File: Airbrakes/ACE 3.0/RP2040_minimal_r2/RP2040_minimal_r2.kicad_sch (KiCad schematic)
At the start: 45 parts, among them J1 USB_B_Micro, J2 Conn_01x02, J3 104031-0811, J4 Conn_02x18_Odd_Even, J5 104031-0811, U1 NCP1117-3.3_SOT223, U2 W25Q128JVS, U3 RP2040, U4 BMI088, U5 BMP581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

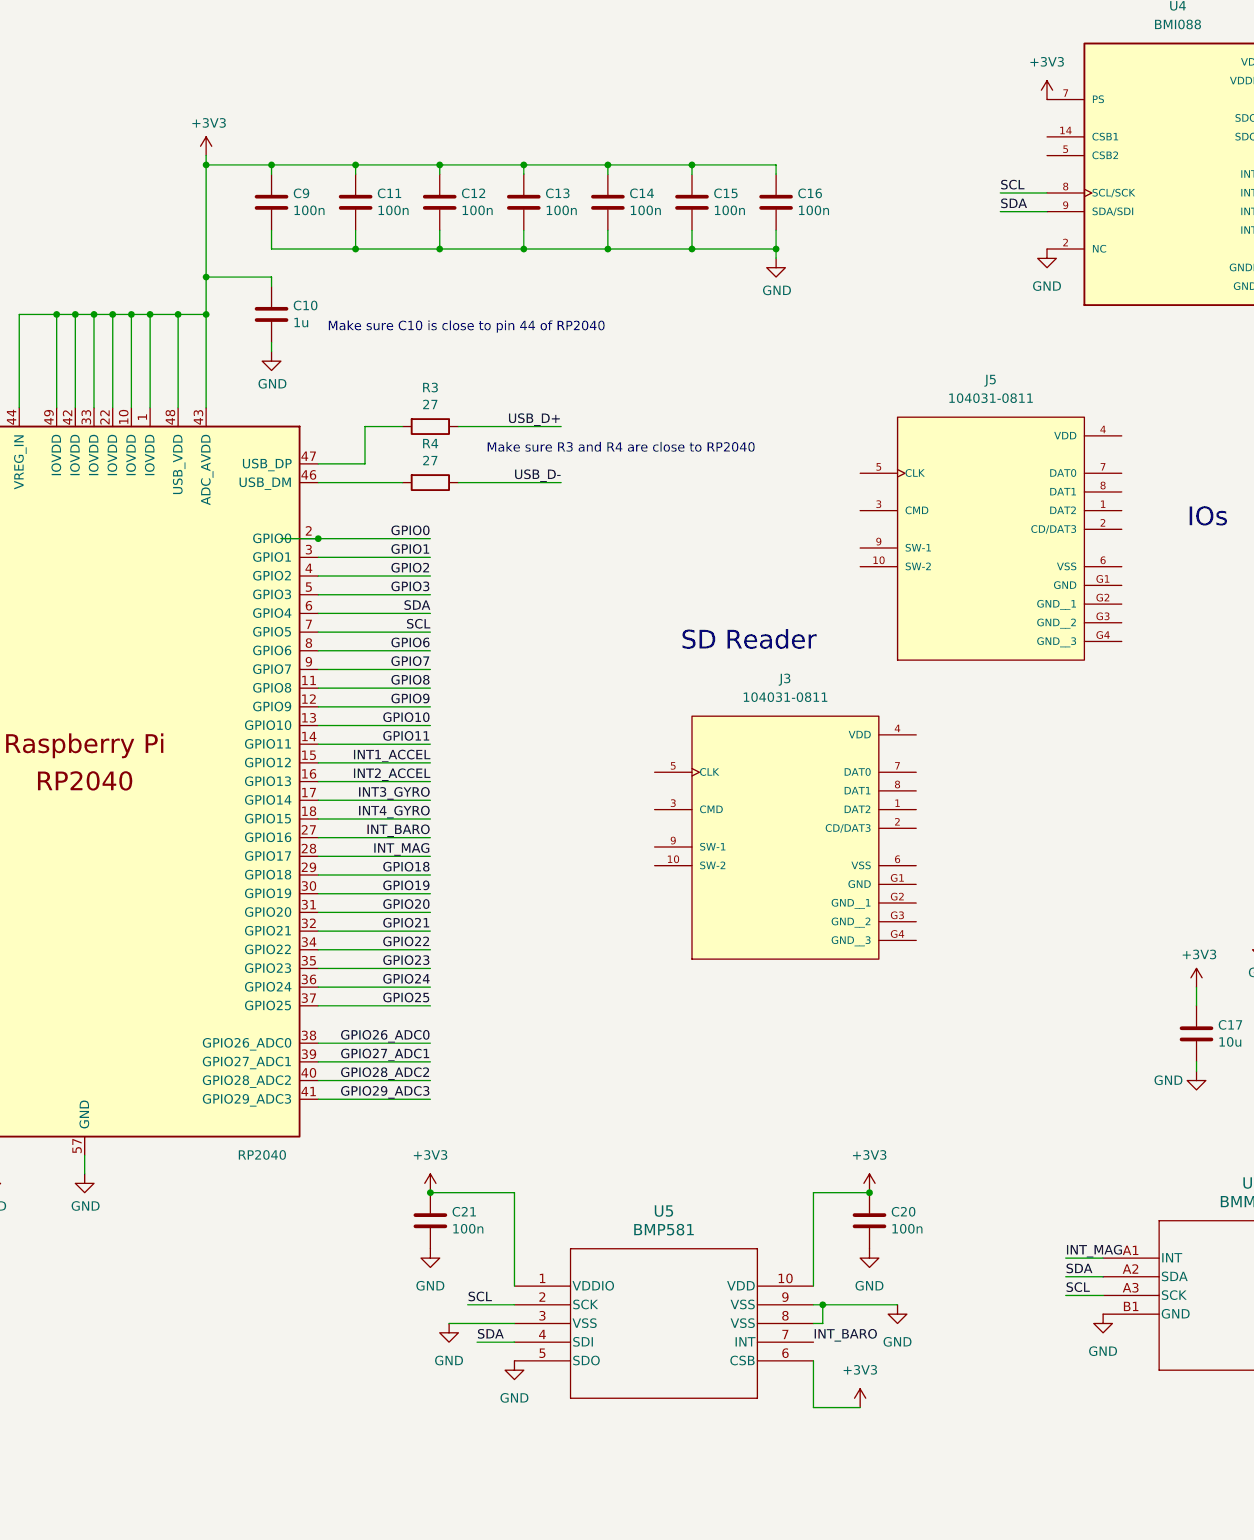
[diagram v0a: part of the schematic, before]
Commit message: Kicad prototype/sd card (#110)
* sd card interfacing

* updated traces

* Update traces

* Updated traces

* Redraw left power plane

* Update RP2040_minimal_r2.kicad_pcb

moved trace test

* Test pour again

* loose wire test

* leela awesome pcb

* changed cs_sd to pull-up and fixed csb

* refilled pcb

* repour plane

* WIP wiring + DRC checks

* Fix gnd connection

* Added resistor value for CS_SD pull up

* New Sensor Board - No pringles

* Ignore .zip

---------

Co-authored-by: breadnmkii <b.z.yang@wustl.edu>
Co-authored-by: leela-srinivas <112487951+leela-srinivas@users.noreply.github.com>
Co-authored-by: wurdahl <44688469+wurdahl@users.noreply.github.com>
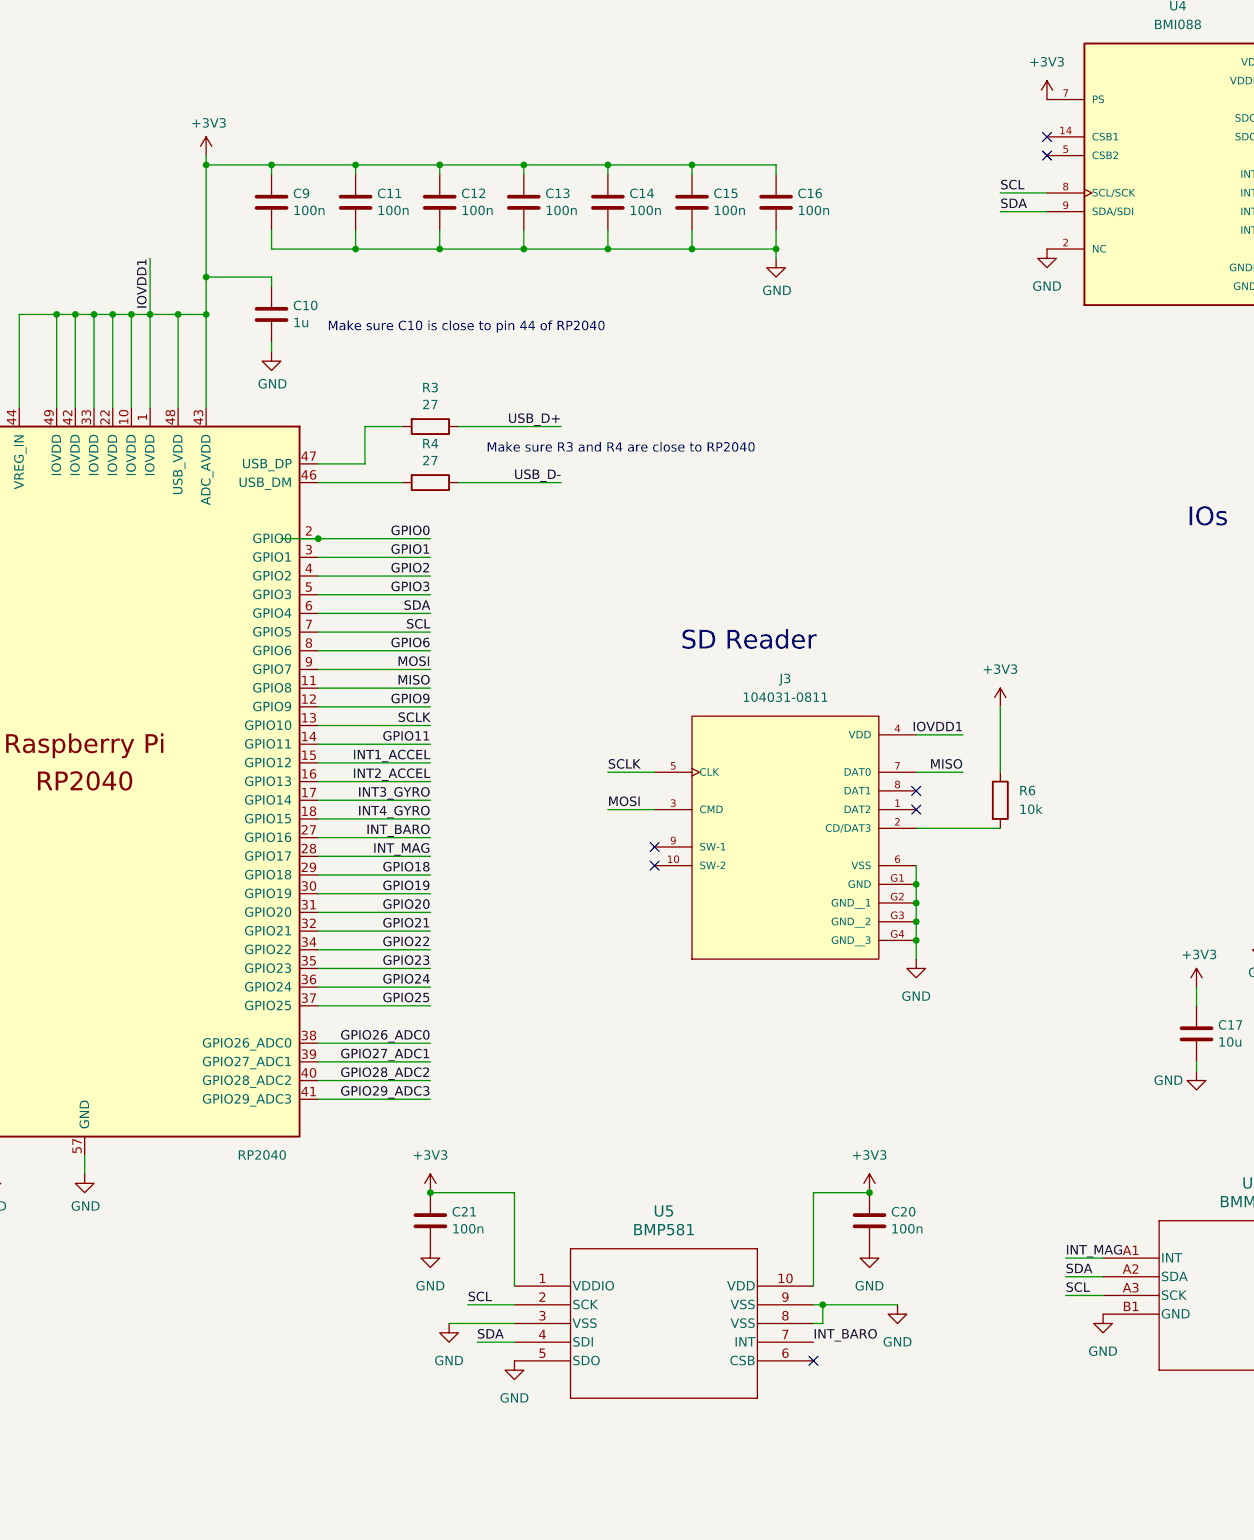
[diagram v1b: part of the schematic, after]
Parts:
- removed J5: 104031-0811, 1040310811-molex_usb:MOLEX_104031-0811, symbol 104031-0811:104031-0811
- added R6: 10k, Resistor_SMD:R_0402_1005Metric, symbol Device:R
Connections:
- net GPIO10 is gone; now on net SCLK: U3.13 (GPIO10)
- net GPIO7 is gone; now on net MOSI: U3.9 (GPIO7)
- net GPIO8 is gone; now on net MISO: U3.11 (GPIO8)
- net +3V3: now also J3.4 (VDD), R6.1; no longer U5.6 (CSB)
- net GND: now also J3.6 (VSS), J3.G1 (GND), J3.G2 (GND__1), J3.G3 (GND__2), J3.G4 (GND__3)
- net at J3.2 (CD/DAT3): now also R6.2
- net MOSI: now reaches J3.3 (CMD)
- net SCLK: now reaches J3.5 (CLK)
- net MISO: now reaches J3.7 (DAT0)
- no-connect marks 1 -> 8
